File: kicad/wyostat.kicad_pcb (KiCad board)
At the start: 2 copper layers, 99.1 x 99.1 mm, 96 parts, among them J1 24 V AC IN, J13 USB_microAB, J16 5V_SEL, J2 OUT1, J3 OUT2, J4 OUT3, J5 I2C_ext1, Q1 BT136-600, Q2 BT136-600, Q3 BT136-600, U1 MOC3063M, U2 MOC3063M, U3 MOC3063M, U4 Wemos-Lolin, U5 MAX17502FATB+T, U6 DS3231N

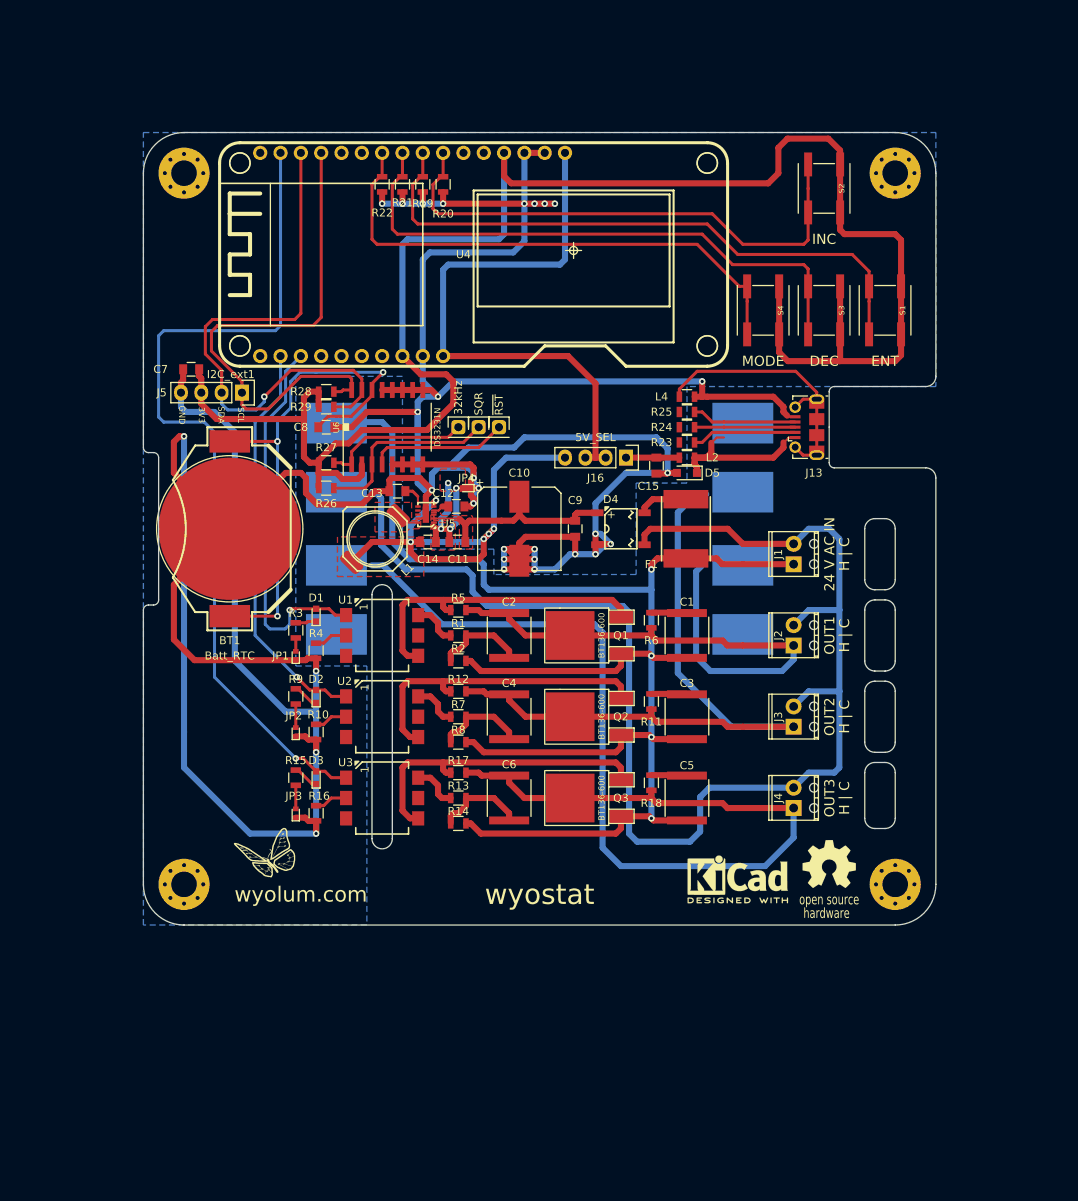
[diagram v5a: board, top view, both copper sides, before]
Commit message: Gerbers ready for OSHpark
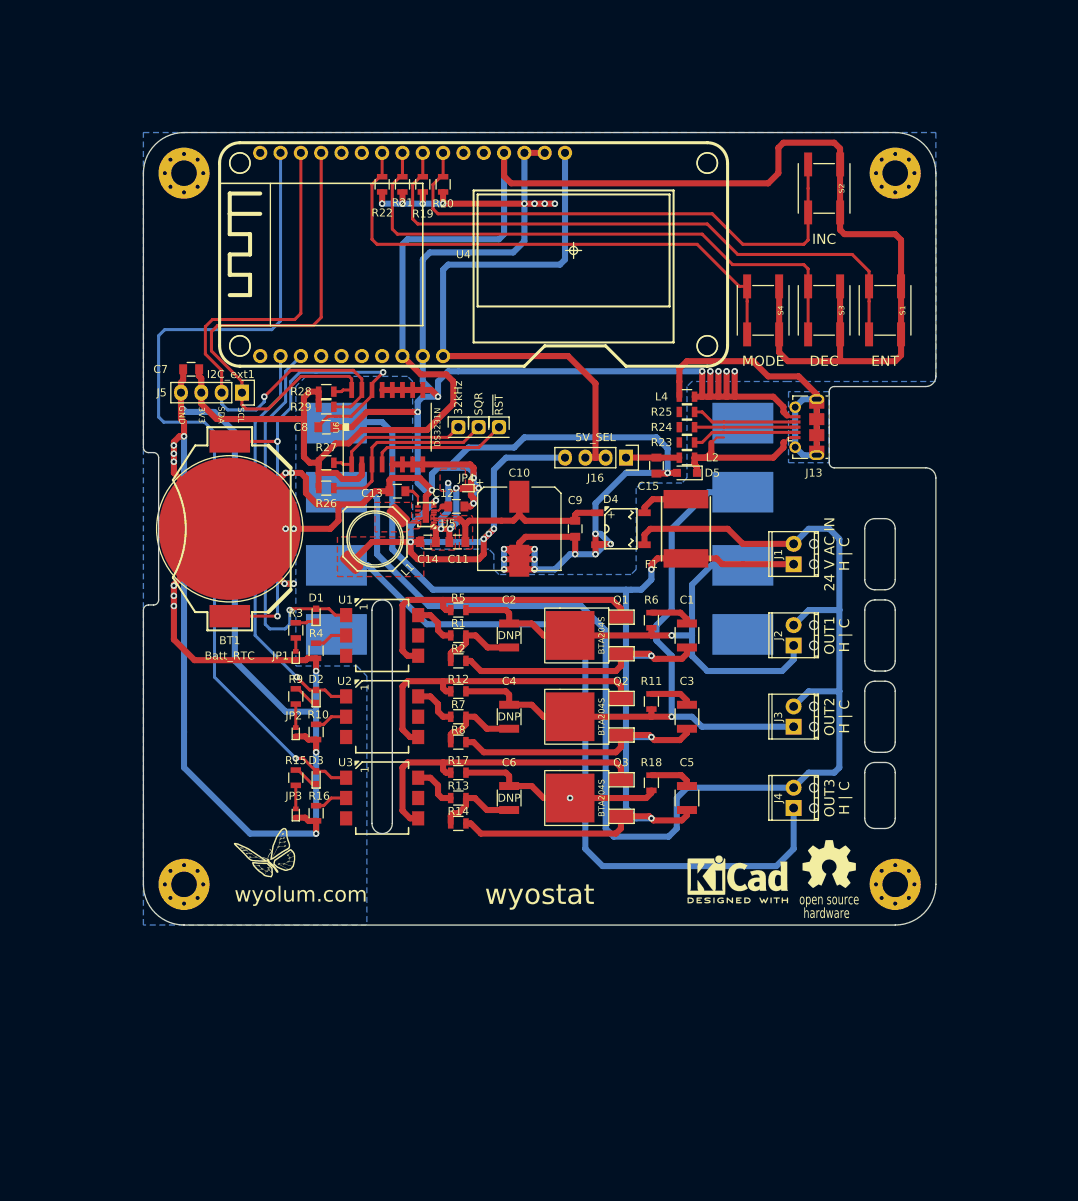
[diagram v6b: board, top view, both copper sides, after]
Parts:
- C1, C2, C3, C4, C5, C6: footprint wyostat_fp:C_2220 -> wyostat_fp:C_1210
- C9: value 100nF -> 100nF,100V
- J10: renamed from REF**; value pad_rect_smd -> Y2
- J11: renamed from REF**; value pad_rect_smd -> G
- J12: renamed from REF**; value pad_rect_smd -> W1
- J14: renamed from REF**; value pad_rect_smd -> W2
- J6: renamed from REF**; value pad_rect_smd -> RH
- J7: renamed from REF**; value pad_rect_smd -> RC
- J8: renamed from REF**; value pad_rect_smd -> C
- J9: renamed from REF**; value pad_rect_smd -> Y1
- Q1, Q2, Q3: value BT136-600 -> BTA204S
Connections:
- J11 pad 1: (no net) -> /OUT2
- J12 pad 1: (no net) -> /OUT3
- J6 pad 1: (no net) -> /24Vac-H
- J8 pad 1: (no net) -> /24Vac-C
- J9 pad 1: (no net) -> /OUT1
- R23 pad 1: /USB_D- -> (no net)
- R24 pad 1: /USB_D+ -> (no net)
- R25 pad 1: /USB_ID -> (no net)
- U1 pad 3: Net-(U1-Pad3) -> (no net)
- U1 pad 5: Net-(U1-Pad5) -> (no net)
- U2 pad 3: Net-(U2-Pad3) -> (no net)
- U2 pad 5: Net-(U2-Pad5) -> (no net)
- U3 pad 3: Net-(U3-Pad3) -> (no net)
- U3 pad 5: Net-(U3-Pad5) -> (no net)
- U4 pad 1: Net-(U4-Pad1) -> (no net)
- U4 pad 11: Net-(U4-Pad11) -> (no net)
- U4 pad 12: Net-(U4-Pad12) -> (no net)
- U4 pad 20: Net-(U4-Pad20) -> (no net)
- U4 pad 21: Net-(U4-Pad21) -> (no net)
- U4 pad 22: Net-(U4-Pad22) -> (no net)
- U4 pad 23: Net-(U4-Pad23) -> (no net)
- U4 pad 26: Net-(U4-Pad26) -> (no net)
- U4 pad 5: Net-(U4-Pad5) -> (no net)
- U4 pad 6: Net-(U4-Pad6) -> (no net)
- U5 pad 7: Net-(U5-Pad7) -> (no net)
- U5 pad 8: /R -> (no net)
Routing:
- net GND: track 542.8 -> 592.0 mm, vias 34 -> 50
- net Net-(J13-PadS1): track 34.2 -> 48.6 mm
- net /OUT3: track 133.6 -> 122.1 mm, vias 0 -> 1
- net /24Vac-H: track 198.2 -> 208.2 mm
- net /OUT1: track 71.2 -> 63.4 mm, vias 0 -> 1
- net /OUT2: track 86.0 -> 80.3 mm, vias 0 -> 1
- net /24Vac-C: track 173.3 -> 174.7 mm
- net Net-(C2-Pad1): track 11.4 -> 10.4 mm
- net Net-(C6-Pad1): track 11.4 -> 10.4 mm
- net Net-(C4-Pad1): track 11.4 -> 10.4 mm
- net Net-(C5-Pad2): track 4.47 -> 5.39 mm
- net Net-(C3-Pad2): track 4.47 -> 5.32 mm
- net Net-(C1-Pad2): track 4.47 -> 5.32 mm
- added copper zone on B.Cu, net Net-(J13-PadS1)
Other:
- outline, holes or cut-outs redrawn
- board text added: "24VAC"
- board text added: "G"
- board text added: "OUT3"
- board text added: "RC"
- board text added: "RH"
- board text added: "W1 O/B"
- board text added: "W2 aux"
- board text added: "Y1"
- board text added: "Y2"
- board text removed: "H"

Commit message: increased clearances, added inverse text
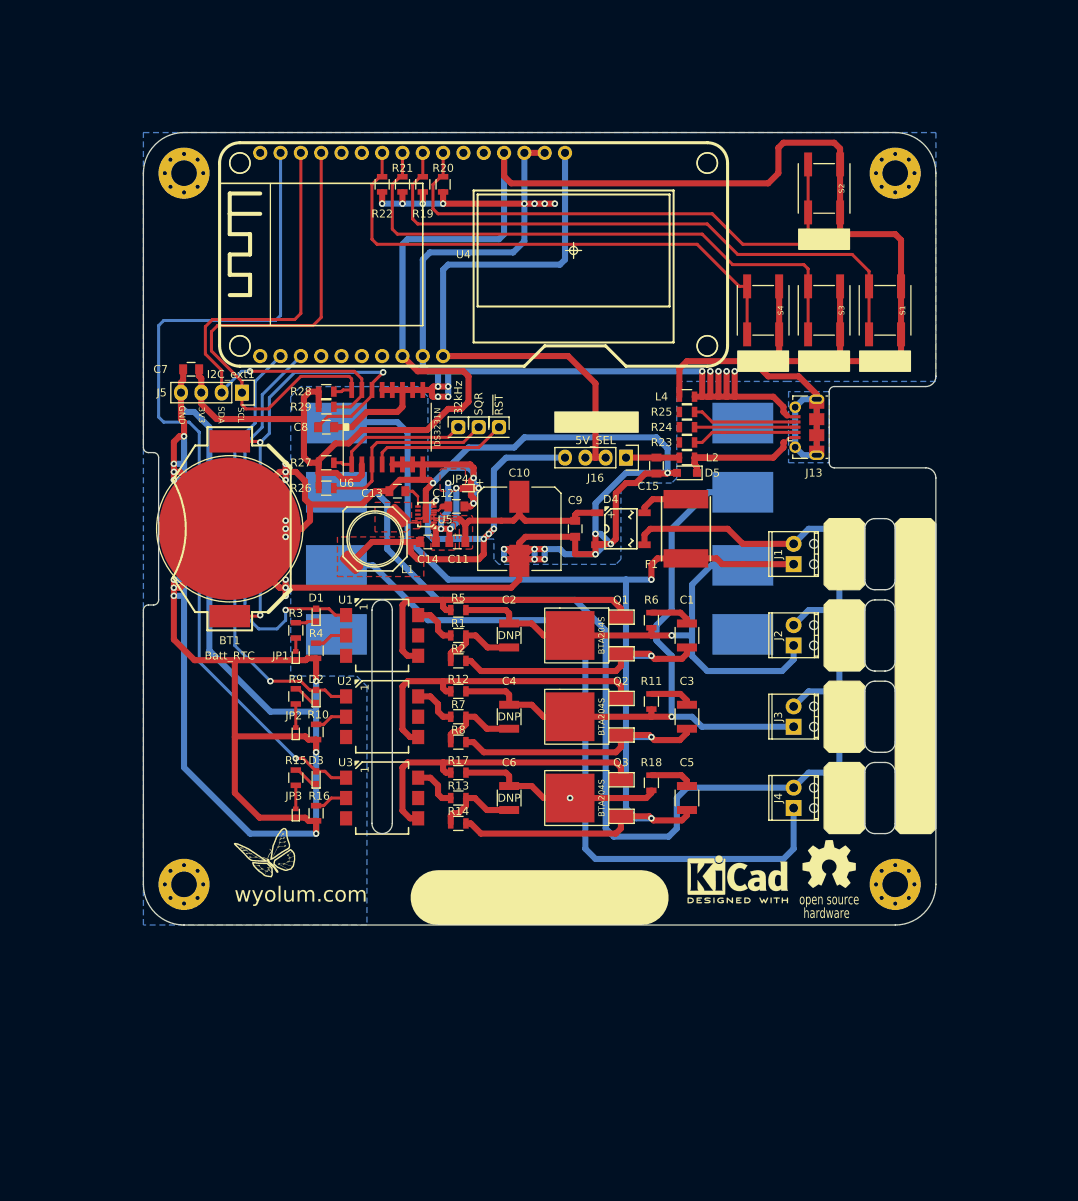
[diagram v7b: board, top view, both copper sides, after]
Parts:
- added Logo4: logo_snb, wyostat_fp:logo-skull_n_bones, B.Cu at (81.3, 81.3)
- Logo1: renamed from G1; footprint wyostat_fp:Logo-WL3 -> wyostat_fp:logo-WL3
- Logo2: renamed from G2; footprint wyostat_fp:OSHW_6mm -> wyostat_fp:logo-OSHW_6mm
- Logo3: renamed from G3; footprint wyostat_fp:KiCad-Logo2_6mm_SilkScreen -> wyostat_fp:logo-kicad_6mm_SilkScreen
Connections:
- J10 pad 1: (no net) -> /Y2
- J14 pad 1: (no net) -> /W2
- J7 pad 1: (no net) -> /Rc
- R23 pad 1: (no net) -> /USB_D-
- R24 pad 1: (no net) -> /USB_D+
- R25 pad 1: (no net) -> /USB_ID
- U1 pad 3: (no net) -> Net-(U1-Pad3)
- U1 pad 5: (no net) -> Net-(U1-Pad5)
- U2 pad 3: (no net) -> Net-(U2-Pad3)
- U2 pad 5: (no net) -> Net-(U2-Pad5)
- U3 pad 3: (no net) -> Net-(U3-Pad3)
- U3 pad 5: (no net) -> Net-(U3-Pad5)
- U4 pad 1: (no net) -> Net-(U4-Pad1)
- U4 pad 11: (no net) -> Net-(U4-Pad11)
- U4 pad 12: (no net) -> Net-(U4-Pad12)
- U4 pad 20: (no net) -> Net-(U4-Pad20)
- U4 pad 21: (no net) -> Net-(U4-Pad21)
- U4 pad 22: (no net) -> Net-(U4-Pad22)
- U4 pad 23: (no net) -> Net-(U4-Pad23)
- U4 pad 26: (no net) -> Net-(U4-Pad26)
- U4 pad 5: (no net) -> Net-(U4-Pad5)
- U4 pad 6: (no net) -> Net-(U4-Pad6)
- U5 pad 7: (no net) -> Net-(U5-Pad7)
- U5 pad 8: (no net) -> /R
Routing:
- net GND: track 592.0 -> 671.5 mm, vias 50 -> 54
- net /IN2: track 50.8 -> 55.1 mm
- net /3V3: track 225.9 -> 229.9 mm
- net /USB+: track 21.5 -> 17.5 mm
- net /5V_IN1: track 59.7 -> 55.8 mm, vias 5 -> 4
- net /rtc_ds3231/BAT: track 65.9 -> 62.8 mm
- net /SDA: track 70.1 -> 67.1 mm
- net /IN1: track 48.1 -> 50.7 mm
- net /IN3: track 107.2 -> 106.4 mm
- net /24Vac-C: track 174.7 -> 173.9 mm
- net /OUT3: track 122.1 -> 121.3 mm
- net /24Vac-H: track 208.2 -> 207.7 mm
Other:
- outline, holes or cut-outs redrawn
- board text added: "24VAC MAX., ISOLATED DO NOT CONNECT 115VAC"
- board text added: "DEC"
- board text added: "ENT"
- board text added: "EXT<OFF>USB"
- board text added: "INC"
- board text added: "MODE"

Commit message: improved silk legend
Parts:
- added G***: LOGO, wyostat_fp:logo-warning, F.Cu at (108.6, 74.3)
- moved Logo1 14.8 mm to (56.0, 122.7)
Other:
- board text added: "J16 OFF when USB connected to ESP32"
